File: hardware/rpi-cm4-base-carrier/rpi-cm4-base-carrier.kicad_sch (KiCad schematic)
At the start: 0 parts

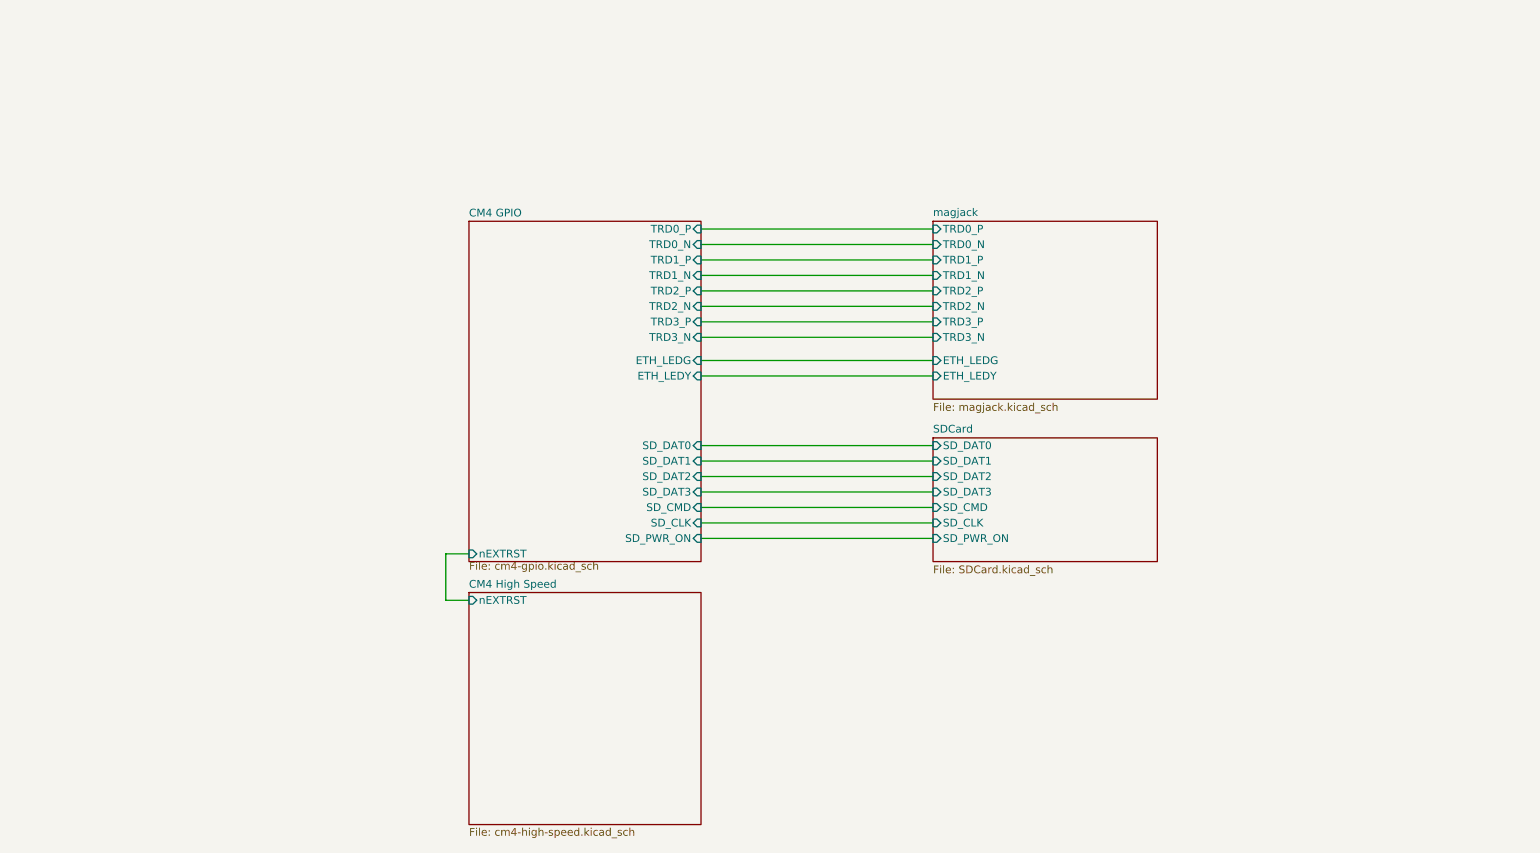
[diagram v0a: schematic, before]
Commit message: schematic entry for samtec board edge connector complete, started breakout of GPIO lines for connection to board edge connector
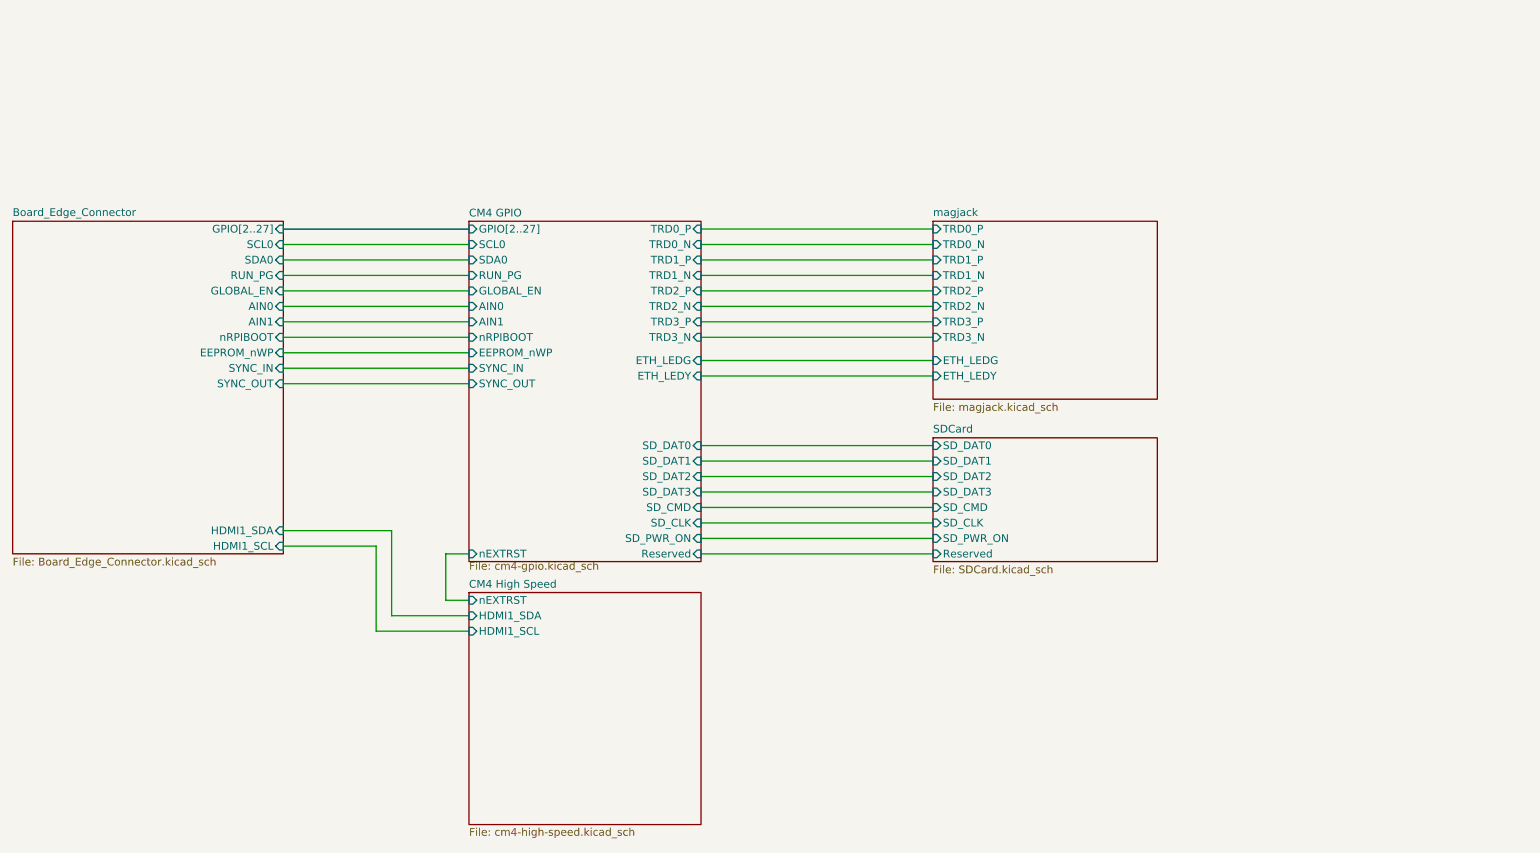
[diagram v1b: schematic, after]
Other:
- added sheet Board_Edge_Connector (Board_Edge_Connector.kicad_sch)
- sheet CM4 GPIO ports: added AIN0, AIN1, EEPROM_nWP, GLOBAL_EN, GPIO[2..27], RUN_PG, Reserved, SCL0, SDA0, SYNC_IN, SYNC_OUT, nRPIBOOT; removed none
- sheet CM4 High Speed ports: added HDMI1_SCL, HDMI1_SDA; removed none
- sheet SDCard ports: added Reserved; removed none
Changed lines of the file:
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@@
+    (stroke (width 0) (type default))
+  )
+  (wire (pts (xy 71.12 62.23) (xy 101.6 62.23))
     (stroke (width 0) (type default))
   )
@@
     (stroke (width 0) (type default))
   )
+  (wire (pts (xy 71.12 57.15) (xy 101.6 57.15))
+    (stroke (width 0) (type default))
+  )
   (wire (pts (xy 139.7 59.69) (xy 177.8 59.69))
     (stroke (width 0) (type default))
@@
     (stroke (width 0) (type default))
   )
+  (wire (pts (xy 88.9 101.6) (xy 71.12 101.6))
+    (stroke (width 0) (type default))
+  )
   (wire (pts (xy 97.79 113.03) (xy 97.79 105.41))
     (stroke (width 0) (type default))
@@
     (stroke (width 0) (type default))
   )
+  (wire (pts (xy 86.36 104.14) (xy 86.36 118.11))
+    (stroke (width 0) (type default))
+  )
   (wire (pts (xy 139.7 76.2) (xy 177.8 76.2))
     (stroke (width 0) (type default))
   )
+  (wire (pts (xy 71.12 54.61) (xy 101.6 54.61))
+    (stroke (width 0) (type default))
+  )
   (wire (pts (xy 139.7 90.17) (xy 177.8 90.17))
     (stroke (width 0) (type default))
   )
+  (wire (pts (xy 101.6 115.57) (xy 88.9 115.57))
+    (stroke (width 0) (type default))
+  )
   (wire (pts (xy 139.7 54.61) (xy 177.8 54.61))
     (stroke (width 0) (type default))
   )
+  (wire (pts (xy 71.12 77.47) (xy 101.6 77.47))
+    (stroke (width 0) (type default))
+  )
+  (wire (pts (xy 88.9 115.57) (xy 88.9 101.6))
+    (stroke (width 0) (type default))
+  )
   (wire (pts (xy 139.7 52.07) (xy 177.8 52.07))
     (stroke (width 0) (type default))
   )
+  (wire (pts (xy 139.7 105.41) (xy 177.8 105.41))
+    (stroke (width 0) (type default))
+  )
   (wire (pts (xy 139.7 64.77) (xy 177.8 64.77))
     (stroke (width 0) (type default))
@@
     (stroke (width 0) (type default))
   )
+  (wire (pts (xy 71.12 72.39) (xy 101.6 72.39))
+    (stroke (width 0) (type default))
+  )
+  (wire (pts (xy 71.12 104.14) (xy 86.36 104.14))
+    (stroke (width 0) (type default))
+  )
+  (wire (pts (xy 71.12 67.31) (xy 101.6 67.31))
+    (stroke (width 0) (type default))
+  )
+  (wire (pts (xy 71.12 59.69) (xy 101.6 59.69))
+    (stroke (width 0) (type default))
+  )
+  (wire (pts (xy 86.36 118.11) (xy 101.6 118.11))
+    (stroke (width 0) (type default))
+  )
   (wire (pts (xy 139.7 57.15) (xy 177.8 57.15))
     (stroke (width 0) (type default))
   )
+  (wire (pts (xy 71.12 74.93) (xy 101.6 74.93))
+    (stroke (width 0) (type default))
+  )
+  (wire (pts (xy 71.12 69.85) (xy 101.6 69.85))
+    (stroke (width 0) (type default))
+  )
+  (bus (pts (xy 71.12 52.07) (xy 101.6 52.07))
+    (stroke (width 0) (type default))
+  )
   (wire (pts (xy 97.79 105.41) (xy 101.6 105.41))
+    (stroke (width 0) (type default))
+  )
+  (wire (pts (xy 71.12 64.77) (xy 101.6 64.77))
     (stroke (width 0) (type default))
   )
@@
       (effects (font (size 1.27 1.27)) (justify left))
     )
+    (pin "Reserved" input (at 177.8 105.41 180)
+      (effects (font (size 1.27 1.27)) (justify left))
+    )
     (instances
       (project "rpi-cm4-base-carrier"
@@
     )
   )
+  (sheet (at 26.67 50.8) (size 44.45 54.61) (fields_autoplaced)
+    (stroke (width 0.1524) (type solid))
+    (fill (color 0 0 0 0.0000))
+    (property "Sheetname" "Board_Edge_Connector" (at 26.67 50.0884 0)
+      (effects (font (size 1.27 1.27)) (justify left bottom))
+    )
+    (property "Sheetfile" "Board_Edge_Connector.kicad_sch" (at 26.67 105.9946 0)
+      (effects (font (size 1.27 1.27)) (justify left top))
+    )
+    (pin "GPIO[2..27]" input (at 71.12 52.07 0)
+      (effects (font (size 1.27 1.27)) (justify right))
+    )
+    (pin "HDMI1_SDA" input (at 71.12 101.6 0)
+      (effects (font (size 1.27 1.27)) (justify right))
+    )
+    (pin "HDMI1_SCL" input (at 71.12 104.14 0)
+      (effects (font (size 1.27 1.27)) (justify right))
+    )
+    (pin "SDA0" input (at 71.12 57.15 0)
+      (effects (font (size 1.27 1.27)) (justify right))
+    )
+    (pin "SCL0" input (at 71.12 54.61 0)
+      (effects (font (size 1.27 1.27)) (justify right))
+    )
+    (pin "RUN_PG" input (at 71.12 59.69 0)
+      (effects (font (size 1.27 1.27)) (justify right))
+    )
+    (pin "GLOBAL_EN" input (at 71.12 62.23 0)
+      (effects (font (size 1.27 1.27)) (justify right))
+    )
+    (pin "AIN1" input (at 71.12 67.31 0)
+      (effects (font (size 1.27 1.27)) (justify right))
+    )
+    (pin "SYNC_IN" input (at 71.12 74.93 0)
+      (effects (font (size 1.27 1.27)) (justify right))
+    )
+    (pin "nRPIBOOT" input (at 71.12 69.85 0)
+      (effects (font (size 1.27 1.27)) (justify right))
+    )
+    (pin "EEPROM_nWP" input (at 71.12 72.39 0)
+      (effects (font (size 1.27 1.27)) (justify right))
+    )
+    (pin "AIN0" input (at 71.12 64.77 0)
+      (effects (font (size 1.27 1.27)) (justify right))
+    )
+    (pin "SYNC_OUT" input (at 71.12 77.47 0)
+      (effects (font (size 1.27 1.27)) (justify right))
+    )
+    (instances
+      (project "rpi-cm4-base-carrier"
+        (path "/92c58705-ecb0-498b-b561-44a3f0daad57" (page "9"))
+      )
+    )
+  )
   (sheet (at 101.6 111.76) (size 38.1 38.1)
     (stroke (width 0) (type solid) (color 132 0 132 1))
@@
       (effects (font (size 1.27 1.27)) (justify left))
     )
+    (pin "HDMI1_SDA" input (at 101.6 115.57 180)
+      (effects (font (size 1.27 1.27)) (justify left))
+    )
+    (pin "HDMI1_SCL" input (at 101.6 118.11 180)
+      (effects (font (size 1.27 1.27)) (justify left))
+    )
     (instances
       (project "rpi-cm4-base-carrier"
@@
       (effects (font (size 1.27 1.27)) (justify left))
     )
+    (pin "Reserved" input (at 139.7 105.41 0)
+      (effects (font (size 1.27 1.27)) (justify right))
+    )
+    (pin "GPIO[2..27]" input (at 101.6 52.07 180)
+      (effects (font (size 1.27 1.27)) (justify left))
+    )
+    (pin "SCL0" input (at 101.6 54.61 180)
+      (effects (font (size 1.27 1.27)) (justify left))
+    )
+    (pin "SDA0" input (at 101.6 57.15 180)
+      (effects (font (size 1.27 1.27)) (justify left))
+    )
+    (pin "EEPROM_nWP" input (at 101.6 72.39 180)
+      (effects (font (size 1.27 1.27)) (justify left))
+    )
+    (pin "nRPIBOOT" input (at 101.6 69.85 180)
+      (effects (font (size 1.27 1.27)) (justify left))
+    )
+    (pin "GLOBAL_EN" input (at 101.6 62.23 180)
+      (effects (font (size 1.27 1.27)) (justify left))
+    )
+    (pin "AIN0" input (at 101.6 64.77 180)
+      (effects (font (size 1.27 1.27)) (justify left))
+    )
+    (pin "AIN1" input (at 101.6 67.31 180)
+      (effects (font (size 1.27 1.27)) (justify left))
+    )
+    (pin "SYNC_OUT" input (at 101.6 77.47 180)
+      (effects (font (size 1.27 1.27)) (justify left))
+    )
+    (pin "SYNC_IN" input (at 101.6 74.93 180)
+      (effects (font (size 1.27 1.27)) (justify left))
+    )
+    (pin "RUN_PG" input (at 101.6 59.69 180)
+      (effects (font (size 1.27 1.27)) (justify left))
+    )

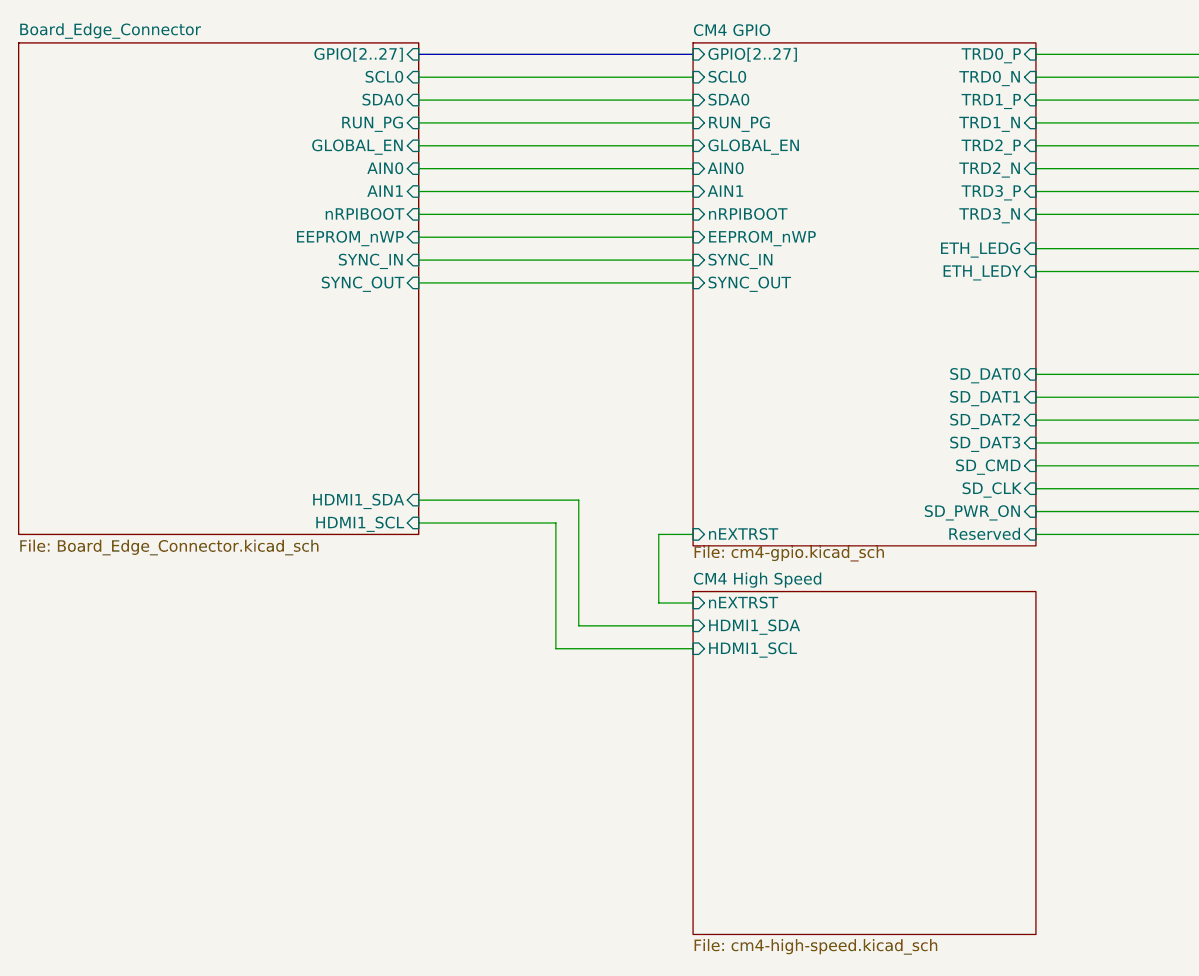
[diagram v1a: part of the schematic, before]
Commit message: redundant USBC power schematic created, layout of single USBC input completed@
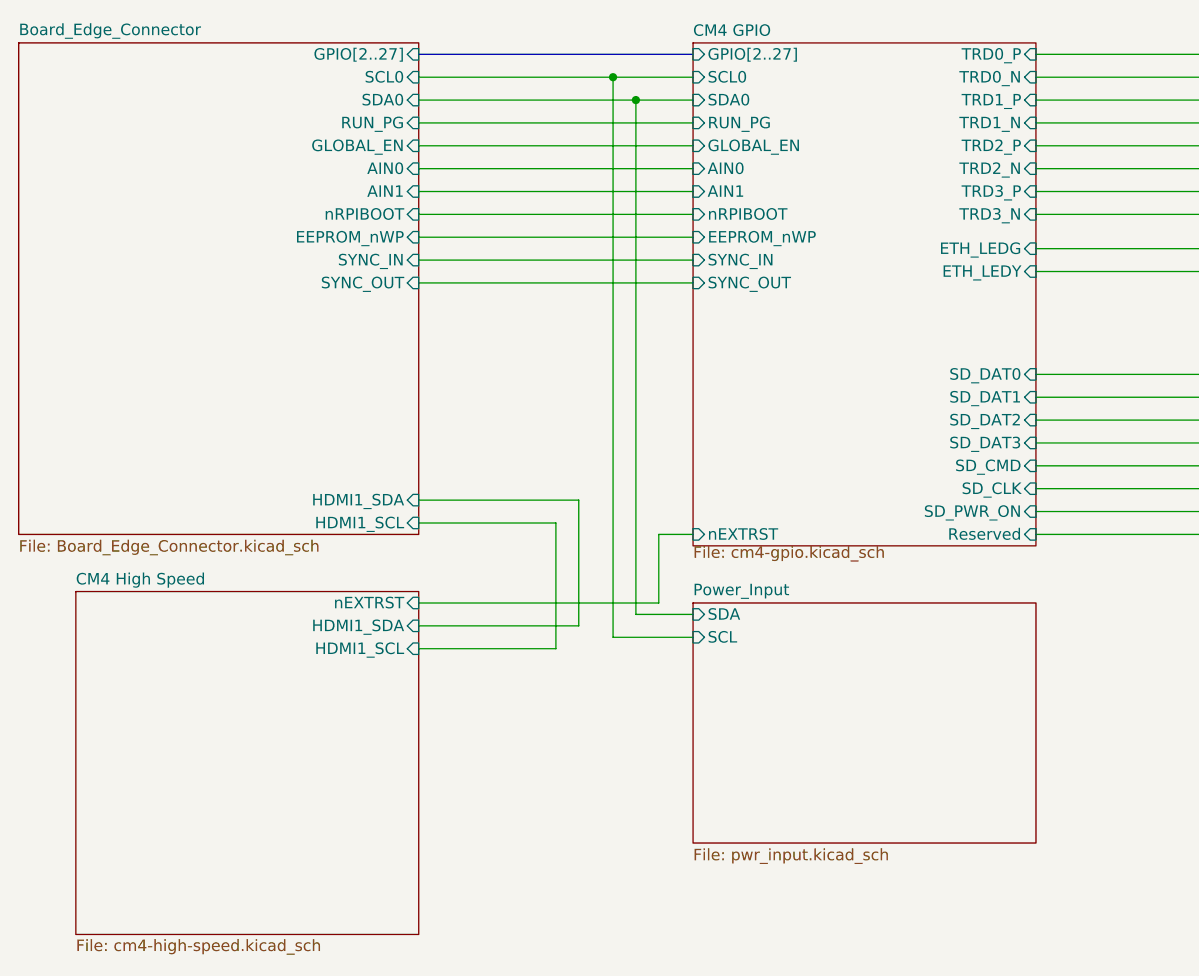
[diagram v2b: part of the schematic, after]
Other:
- added sheet Power_Input (pwr_input.kicad_sch)
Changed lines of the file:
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@@
     (comment 4 "Author: Shawn Hymel")
   )
+  (junction (at 92.71 54.61) (diameter 0) (color 0 0 0 0)
+  )
+  (junction (at 95.25 57.15) (diameter 0) (color 0 0 0 0)
+  )
   (wire (pts (xy 139.7 62.23) (xy 177.8 62.23))
     (stroke (width 0) (type default))
@@
     (stroke (width 0) (type default))
   )
+  (wire (pts (xy 95.25 114.3) (xy 95.25 57.15))
+    (stroke (width 0) (type default))
+  )
   (wire (pts (xy 139.7 97.79) (xy 177.8 97.79))
     (stroke (width 0) (type default))
   )
-  (wire (pts (xy 101.6 113.03) (xy 97.79 113.03))
+  (wire (pts (xy 71.12 113.03) (xy 97.79 113.03))
     (stroke (width 0) (type default))
   )
@@
     (stroke (width 0) (type default))
   )
-  (wire (pts (xy 71.12 57.15) (xy 101.6 57.15))
+  (wire (pts (xy 71.12 57.15) (xy 95.25 57.15))
+    (stroke (width 0) (type default))
+  )
+  (wire (pts (xy 101.6 114.3) (xy 95.25 114.3))
     (stroke (width 0) (type default))
   )
@@
     (stroke (width 0) (type default))
   )
+  (wire (pts (xy 101.6 116.84) (xy 92.71 116.84))
+    (stroke (width 0) (type default))
+  )
   (wire (pts (xy 139.7 76.2) (xy 177.8 76.2))
     (stroke (width 0) (type default))
   )
-  (wire (pts (xy 71.12 54.61) (xy 101.6 54.61))
+  (wire (pts (xy 71.12 54.61) (xy 92.71 54.61))
     (stroke (width 0) (type default))
   )
@@
     (stroke (width 0) (type default))
   )
-  (wire (pts (xy 101.6 115.57) (xy 88.9 115.57))
+  (wire (pts (xy 71.12 115.57) (xy 88.9 115.57))
     (stroke (width 0) (type default))
   )
@@
     (stroke (width 0) (type default))
   )
+  (wire (pts (xy 95.25 57.15) (xy 101.6 57.15))
+    (stroke (width 0) (type default))
+  )
   (wire (pts (xy 71.12 72.39) (xy 101.6 72.39))
     (stroke (width 0) (type default))
@@
     (stroke (width 0) (type default))
   )
-  (wire (pts (xy 86.36 118.11) (xy 101.6 118.11))
+  (wire (pts (xy 86.36 118.11) (xy 71.12 118.11))
+    (stroke (width 0) (type default))
+  )
+  (wire (pts (xy 92.71 116.84) (xy 92.71 54.61))
     (stroke (width 0) (type default))
   )
@@
   )
   (wire (pts (xy 97.79 105.41) (xy 101.6 105.41))
+    (stroke (width 0) (type default))
+  )
+  (wire (pts (xy 92.71 54.61) (xy 101.6 54.61))
     (stroke (width 0) (type default))
   )
@@
     )
   )
-  (sheet (at 101.6 111.76) (size 38.1 38.1)
+  (sheet (at 101.6 113.03) (size 38.1 26.67) (fields_autoplaced)
+    (stroke (width 0.1524) (type solid))
+    (fill (color 0 0 0 0.0000))
+    (property "Sheetname" "Power_Input" (at 101.6 112.3184 0)
+      (effects (font (size 1.27 1.27)) (justify left bottom))
+    )
+    (property "Sheetfile" "pwr_input.kicad_sch" (at 101.6 140.2846 0)
+      (effects (font (size 1.27 1.27)) (justify left top))
+    )
+    (property "Field2" "" (at 101.6 113.03 0)
+      (effects (font (size 1.27 1.27)) hide)
+    )
+    (pin "SDA" input (at 101.6 114.3 180)
+      (effects (font (size 1.27 1.27)) (justify left))
+    )
+    (pin "SCL" input (at 101.6 116.84 180)
+      (effects (font (size 1.27 1.27)) (justify left))
+    )
+    (instances
+      (project "rpi-cm4-base-carrier"
+        (path "/92c58705-ecb0-498b-b561-44a3f0daad57" (page "12"))
+      )
+    )
+  )
+  (sheet (at 33.02 111.76) (size 38.1 38.1)
     (stroke (width 0) (type solid) (color 132 0 132 1))
     (fill (color 255 255 255 0.0000))
-    (property "Sheetname" "CM4 High Speed" (at 101.6 111.1245 0)
-      (effects (font (size 1.27 1.27)) (justify left bottom))
-    )
-    (property "Sheetfile" "cm4-high-speed.kicad_sch" (at 101.6 150.3685 0)
-      (effects (font (size 1.27 1.27)) (justify left top))
-    )
-    (pin "nEXTRST" input (at 101.6 113.03 180)
-      (effects (font (size 1.27 1.27)) (justify left))
-    )
-    (pin "HDMI1_SDA" input (at 101.6 115.57 180)
-      (effects (font (size 1.27 1.27)) (justify left))
-    )
-    (pin "HDMI1_SCL" input (at 101.6 118.11 180)
-      (effects (font (size 1.27 1.27)) (justify left))
-    )
-    (instances
+    (property "Sheetname" "CM4 High Speed" (at 33.02 111.1245 0)
+      (effects (font (size 1.27 1.27)) (justify left bottom))
+    )
+    (property "Sheetfile" "cm4-high-speed.kicad_sch" (at 33.02 150.3685 0)
+      (effects (font (size 1.27 1.27)) (justify left top))
+    )
+    (pin "nEXTRST" input (at 71.12 113.03 0)
+      (effects (font (size 1.27 1.27)) (justify right))
+    )
+    (pin "HDMI1_SDA" input (at 71.12 115.57 0)
+      (effects (font (size 1.27 1.27)) (justify right))
+    )
+    (pin "HDMI1_SCL" input (at 71.12 118.11 0)
+      (effects (font (size 1.27 1.27)) (justify right))
+    )
+    (instances
